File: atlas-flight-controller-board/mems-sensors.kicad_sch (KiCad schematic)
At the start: 11 parts, among them IC1 LSM6DSV80XTR, IC2 LPS22HHTR, U1 LIS2MDL

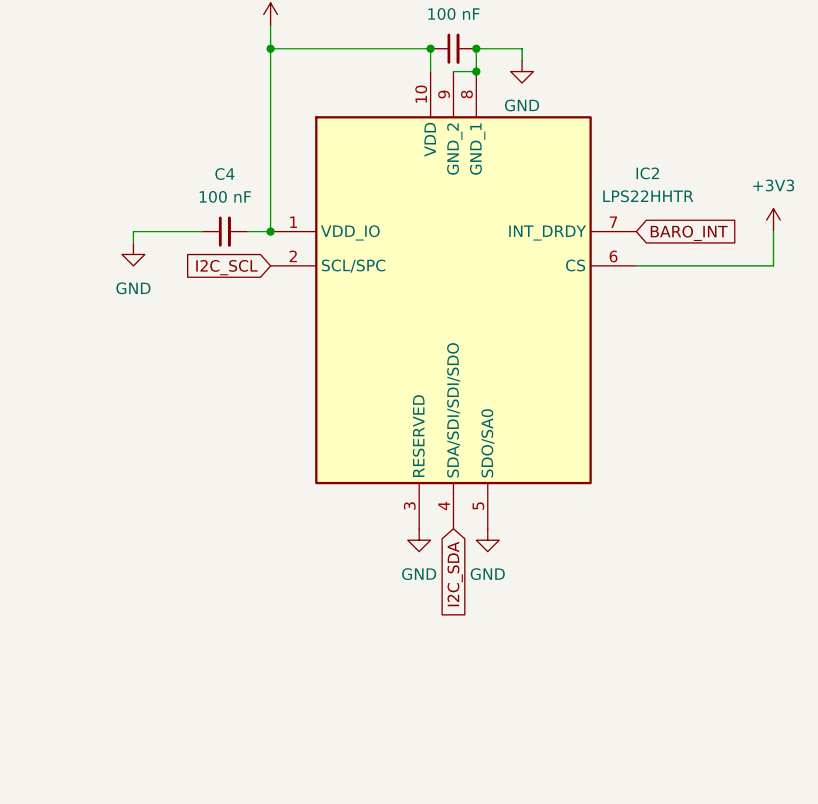
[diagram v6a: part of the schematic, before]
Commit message: Converted BARO to SPI
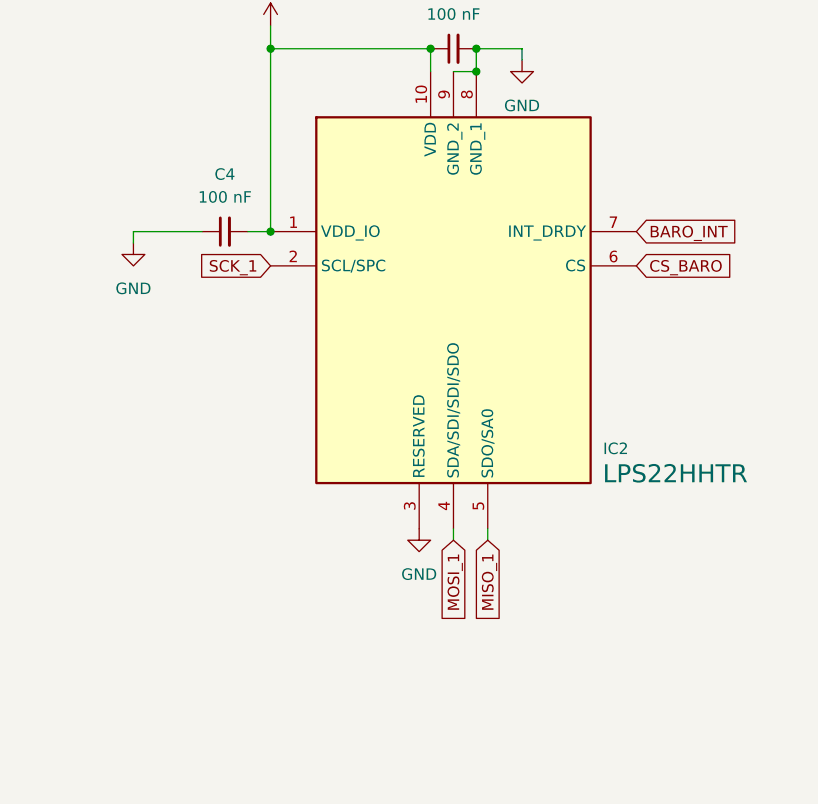
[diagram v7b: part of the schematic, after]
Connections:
- net +3V3: no longer IC2.6 (CS)
- net GND: no longer IC2.5 (SDO/SA0)
- net I2C_SCL: no longer IC2.2 (SCL/SPC)
- net I2C_SDA: no longer IC2.4 (SDA/SDI/SDI/SDO)
- net MISO_1: now also IC2.5 (SDO/SA0)
- net MOSI_1: now also IC2.4 (SDA/SDI/SDI/SDO)
- net SCK_1: now also IC2.2 (SCL/SPC)
- new net CS_BARO: IC2.6 (CS)
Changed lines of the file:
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@@
+	(wire
+		(pts
+			(xy 203.2 95.25) (xy 203.2 93.98)
+		)
+		(stroke
+			(width 0)
+			(type default)
+		)
+	)
 	(wire
 		(pts
@@
 	(wire
 		(pts
+			(xy 207.01 93.98) (xy 207.01 95.25)
+		)
+		(stroke
+			(width 0)
+			(type default)
+		)
+	)
+	(wire
+		(pts
 			(xy 182.88 40.64) (xy 182.88 60.96)
 		)
@@
 	(wire
 		(pts
-			(xy 223.52 64.77) (xy 238.76 64.77)
-		)
-		(stroke
-			(width 0)
-			(type default)
-		)
-	)
-	(wire
-		(pts
 			(xy 81.28 87.63) (xy 83.82 87.63)
 		)
@@
 		(pts
 			(xy 105.41 148.59) (xy 107.95 148.59)
-		)
-		(stroke
-			(width 0)
-			(type default)
-		)
-	)
-	(wire
-		(pts
-			(xy 238.76 60.96) (xy 238.76 64.77)
 		)
 		(stroke
@@
 		)
 	)
+	(global_label "MISO_1"
+		(shape input)
+		(at 207.01 95.25 270)
+		(fields_autoplaced yes)
+		(effects
+			(font
+				(size 1.27 1.27)
+			)
+			(justify right)
+		)
+		(property "Intersheetrefs" "${INTERSHEET_REFS}"
+			(at 207.01 105.0085 90)
+			(effects
+				(font
+					(size 1.27 1.27)
+				)
+				(justify right)
+				(hide yes)
+			)
+		)
+	)
 	(global_label "SCK_1"
 		(shape input)
@@
 		)
 	)
-	(global_label "I2C_SDA"
+	(global_label "MOSI_1"
 		(shape input)
-		(at 203.2 93.98 270)
+		(at 203.2 95.25 270)
 		(fields_autoplaced yes)
 		(effects
@@
 		)
 		(property "Intersheetrefs" "${INTERSHEET_REFS}"
-			(at 203.2 104.5852 90)
+			(at 203.2 105.0085 90)
 			(effects
 				(font
@@
 		)
 	)
-	(global_label "I2C_SCL"
+	(global_label "SCK_1"
 		(shape input)
 		(at 182.88 64.77 180)
@@
 		)
 		(property "Intersheetrefs" "${INTERSHEET_REFS}"
-			(at 172.3353 64.77 0)
+			(at 173.9682 64.77 0)
 			(effects
 				(font
@@
 				)
 				(justify right)
+				(hide yes)
+			)
+		)
+	)
+	(global_label "CS_BARO"
+		(shape input)
+		(at 223.52 64.77 0)
+		(fields_autoplaced yes)
+		(effects
+			(font
+				(size 1.27 1.27)
+			)
+			(justify left)
+		)
+		(property "Intersheetrefs" "${INTERSHEET_REFS}"
+			(at 234.9114 64.77 0)
+			(effects
+				(font
+					(size 1.27 1.27)
+				)
+				(justify left)
 				(hide yes)
 			)
@@
 		(on_board yes)
 		(dnp no)
-		(fields_autoplaced yes)
 		(property "Reference" "IC2"
-			(at 224.79 54.5398 0)
+			(at 221.234 85.09 0)
 			(effects
 				(font
@@
 		)
 		(property "Value" "LPS22HHTR"
-			(at 224.79 57.0798 0)
-			(effects
-				(font
-					(size 1.27 1.27)
+			(at 227.838 87.884 0)
+			(effects
+				(font
+					(size 2 2)
 				)
 			)
@@
 	)
 	(symbol
-		(lib_id "power:GND")
-		(at 207.01 93.98 0)
-		(unit 1)
-		(exclude_from_sim no)
-		(in_bom yes)
-		(on_board yes)
-		(dnp no)
-		(fields_autoplaced yes)
-		(property "Reference" "#PWR0106"
-			(at 207.01 100.33 0)
-			(effects
-				(font
-					(size 1.27 1.27)
-				)
-				(hide yes)
-			)
-		)
-		(property "Value" "GND"
-			(at 207.01 99.06 0)
-			(effects
-				(font
-					(size 1.27 1.27)
-				)
-			)
-		)
-		(property "Footprint" ""
-			(at 207.01 93.98 0)
-			(effects
-				(font
-					(size 1.27 1.27)
-				)
-				(hide yes)
-			)
-		)
-		(property "Datasheet" ""
-			(at 207.01 93.98 0)
-			(effects
-				(font
-					(size 1.27 1.27)
-				)
-				(hide yes)
-			)
-		)
-		(property "Description" "Power symbol creates a global label with name \"GND\" , ground"
-			(at 207.01 93.98 0)
-			(effects
-				(font
-					(size 1.27 1.27)
-				)
-				(hide yes)
-			)
-		)
-		(pin "1"
-		)
-		(instances
-			(project "atlas-flight-controller-board"
-				(path "/99efb2d6-b5f7-438c-9ed2-f359400f01a1/5584e1ef-6e93-420a-9bdf-15a5926ce2b3"
-					(reference "#PWR0106")
-					(unit 1)
-				)
-			)
-		)
-	)
-	(symbol
 		(lib_id "Device:C_Small")
 		(at 113.03 73.66 0)
@@
 					(unit 1)
 				)
-			)
-		)
-	)
-	(symbol
-		(lib_id "power:+3V3")
-		(at 238.76 60.96 0)
-		(unit 1)
-		(exclude_from_sim no)
-		(in_bom yes)
-		(on_board yes)
-		(dnp no)
-		(fields_autoplaced yes)
-		(property "Reference" "#PWR0104"
-			(at 238.76 64.77 0)
-			(effects
-				(font
-					(size 1.27 1.27)
-				)
-				(hide yes)
-			)
-		)
-		(property "Value" "+3V3"
-			(at 238.76 55.88 0)
-			(effects
-				(font
-					(size 1.27 1.27)
-				)
-			)
-		)
-		(property "Footprint" ""
-			(at 238.76 60.96 0)
-			(effects
-				(font
-					(size 1.27 1.27)
-				)
-				(hide yes)
-			)
-		)
-		(property "Datasheet" ""
-			(at 238.76 60.96 0)
-			(effects
-				(font
-					(size 1.27 1.27)
-				)
-				(hide yes)
-			)
-		)
-		(property "Description" "Power symbol creates a global label with name \"+3V3\""
-			(at 238.76 60.96 0)
-			(effects
-				(font
-					(size 1.27 1.27)
-				)
-				(hide yes)
-			)
-		)
-		(pin "1"
-		)
-		(instances
-			(project "atlas-flight-controller-board"
-				(path "/99efb2d6-b5f7-438c-9ed2-f359400f01a1/5584e1ef-6e93-420a-9bdf-15a5926ce2b3"
-					(reference "#PWR0104")
-					(unit 1)
-				)

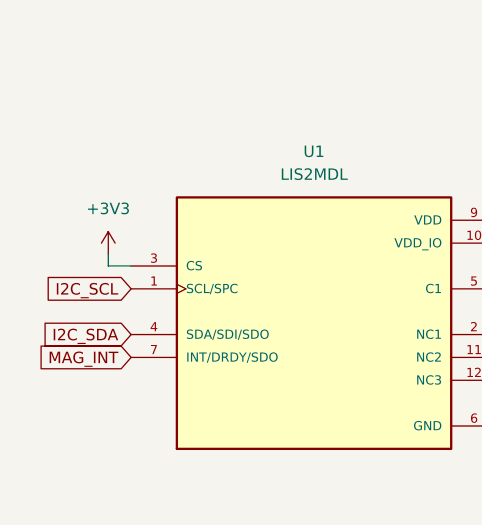
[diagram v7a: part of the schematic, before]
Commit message: Converting MAG to SPI. Have to remove Mag_Int to replace with SDO/MISO pin.
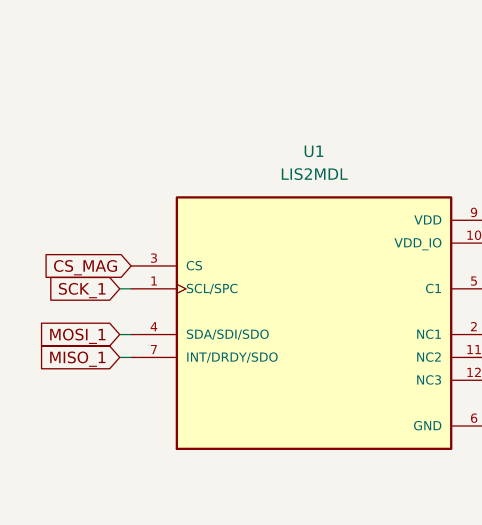
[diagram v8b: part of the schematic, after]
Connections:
- net I2C_SCL is gone; now on net SCK_1: U1.1 (SCL/SPC)
- net I2C_SDA is gone; now on net MOSI_1: U1.4 (SDA/SDI/SDO)
- net MAG_INT is gone; now on net MISO_1: U1.7 (INT/DRDY/SDO)
- net +3V3: no longer U1.3 (CS)
- new net CS_MAG: U1.3 (CS)
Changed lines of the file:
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@@
+	(wire
+		(pts
+			(xy 53.34 161.29) (xy 54.61 161.29)
+		)
+		(stroke
+			(width 0)
+			(type default)
+		)
+	)
 	(wire
 		(pts
@@
 	(wire
 		(pts
-			(xy 52.07 149.86) (xy 52.07 151.13)
-		)
-		(stroke
-			(width 0)
-			(type default)
-		)
-	)
-	(wire
-		(pts
 			(xy 203.2 95.25) (xy 203.2 93.98)
 		)
@@
 	(wire
 		(pts
+			(xy 53.34 158.75) (xy 54.61 158.75)
+		)
+		(stroke
+			(width 0)
+			(type default)
+		)
+	)
+	(wire
+		(pts
 			(xy 207.01 93.98) (xy 207.01 95.25)
 		)
@@
 	(wire
 		(pts
+			(xy 53.34 153.67) (xy 54.61 153.67)
+		)
+		(stroke
+			(width 0)
+			(type default)
+		)
+	)
+	(wire
+		(pts
 			(xy 81.28 87.63) (xy 83.82 87.63)
 		)
@@
 	(wire
 		(pts
-			(xy 54.61 151.13) (xy 52.07 151.13)
-		)
-		(stroke
-			(width 0)
-			(type default)
-		)
-	)
-	(wire
-		(pts
 			(xy 182.88 38.1) (xy 182.88 40.64)
 		)
@@
 		)
 	)
-	(global_label "I2C_SCL"
+	(global_label "SCK_1"
 		(shape input)
-		(at 54.61 153.67 180)
+		(at 53.34 153.67 180)
 		(fields_autoplaced yes)
 		(effects
@@
 		)
 		(property "Intersheetrefs" "${INTERSHEET_REFS}"
-			(at 44.0653 153.67 0)
+			(at 44.4282 153.67 0)
 			(effects
 				(font
@@
 		)
 	)
+	(global_label "CS_MAG"
+		(shape input)
+		(at 54.61 151.13 180)
+		(fields_autoplaced yes)
+		(effects
+			(font
+				(size 1.27 1.27)
+			)
+			(justify right)
+		)
+		(property "Intersheetrefs" "${INTERSHEET_REFS}"
+			(at 44.3677 151.13 0)
+			(effects
+				(font
+					(size 1.27 1.27)
+				)
+				(justify right)
+				(hide yes)
+			)
+		)
+	)
 	(global_label "MOSI_1"
 		(shape input)
@@
 		)
 	)
-	(global_label "MAG_INT"
+	(global_label "MISO_1"
 		(shape input)
-		(at 54.61 161.29 180)
+		(at 53.34 161.29 180)
 		(fields_autoplaced yes)
 		(effects
@@
 		)
 		(property "Intersheetrefs" "${INTERSHEET_REFS}"
-			(at 43.9443 161.29 0)
+			(at 43.5815 161.29 0)
 			(effects
 				(font
@@
 		)
 	)
-	(global_label "I2C_SDA"
+	(global_label "MOSI_1"
 		(shape input)
-		(at 54.61 158.75 180)
+		(at 53.34 158.75 180)
 		(fields_autoplaced yes)
 		(effects
@@
 		)
 		(property "Intersheetrefs" "${INTERSHEET_REFS}"
-			(at 44.0048 158.75 0)
+			(at 43.5815 158.75 0)
 			(effects
 				(font
@@
 					(unit 1)
 				)
-			)
-		)
-	)
-	(symbol
-		(lib_id "power:+3V3")
-		(at 52.07 149.86 0)
-		(unit 1)
-		(exclude_from_sim no)
-		(in_bom yes)
-		(on_board yes)
-		(dnp no)
-		(fields_autoplaced yes)
-		(property "Reference" "#PWR0111"
-			(at 52.07 153.67 0)
-			(effects
-				(font
-					(size 1.27 1.27)
-				)
-				(hide yes)
-			)
-		)
-		(property "Value" "+3V3"
-			(at 52.07 144.78 0)
-			(effects
-				(font
-					(size 1.27 1.27)
-				)
-			)
-		)
-		(property "Footprint" ""
-			(at 52.07 149.86 0)
-			(effects
-				(font
-					(size 1.27 1.27)
-				)
-				(hide yes)
-			)
-		)
-		(property "Datasheet" ""
-			(at 52.07 149.86 0)
-			(effects
-				(font
-					(size 1.27 1.27)
-				)
-				(hide yes)
-			)
-		)
-		(property "Description" "Power symbol creates a global label with name \"+3V3\""
-			(at 52.07 149.86 0)
-			(effects
-				(font
-					(size 1.27 1.27)
-				)
-				(hide yes)
-			)
-		)
-		(pin "1"
-		)
-		(instances
-			(project "atlas-flight-controller-board"
-				(path "/99efb2d6-b5f7-438c-9ed2-f359400f01a1/5584e1ef-6e93-420a-9bdf-15a5926ce2b3"
-					(reference "#PWR0111")
-					(unit 1)
-				)
